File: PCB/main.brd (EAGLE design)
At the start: 98.1 x 68.5 mm, 81 parts, among them X1 BU-SMA-V

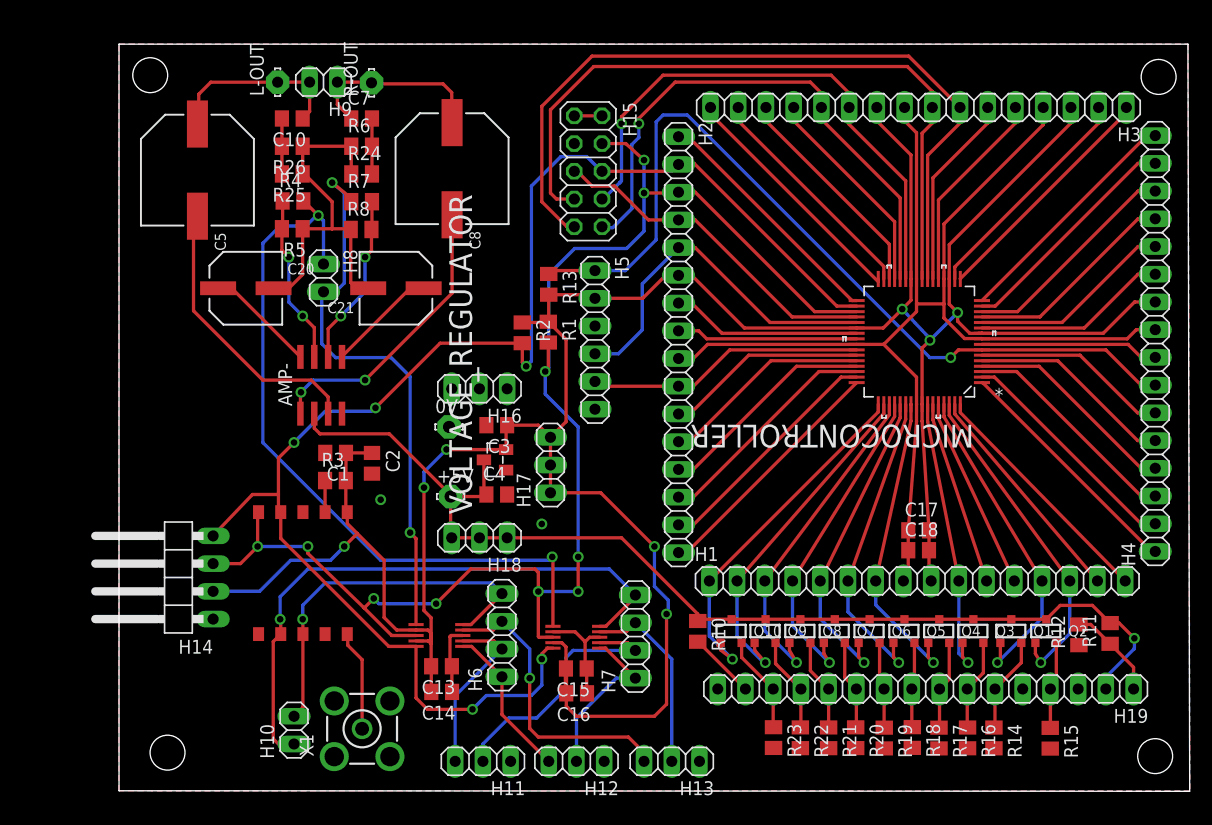
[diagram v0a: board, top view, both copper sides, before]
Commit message: "Final" PCB changes
Changes from group PCB review
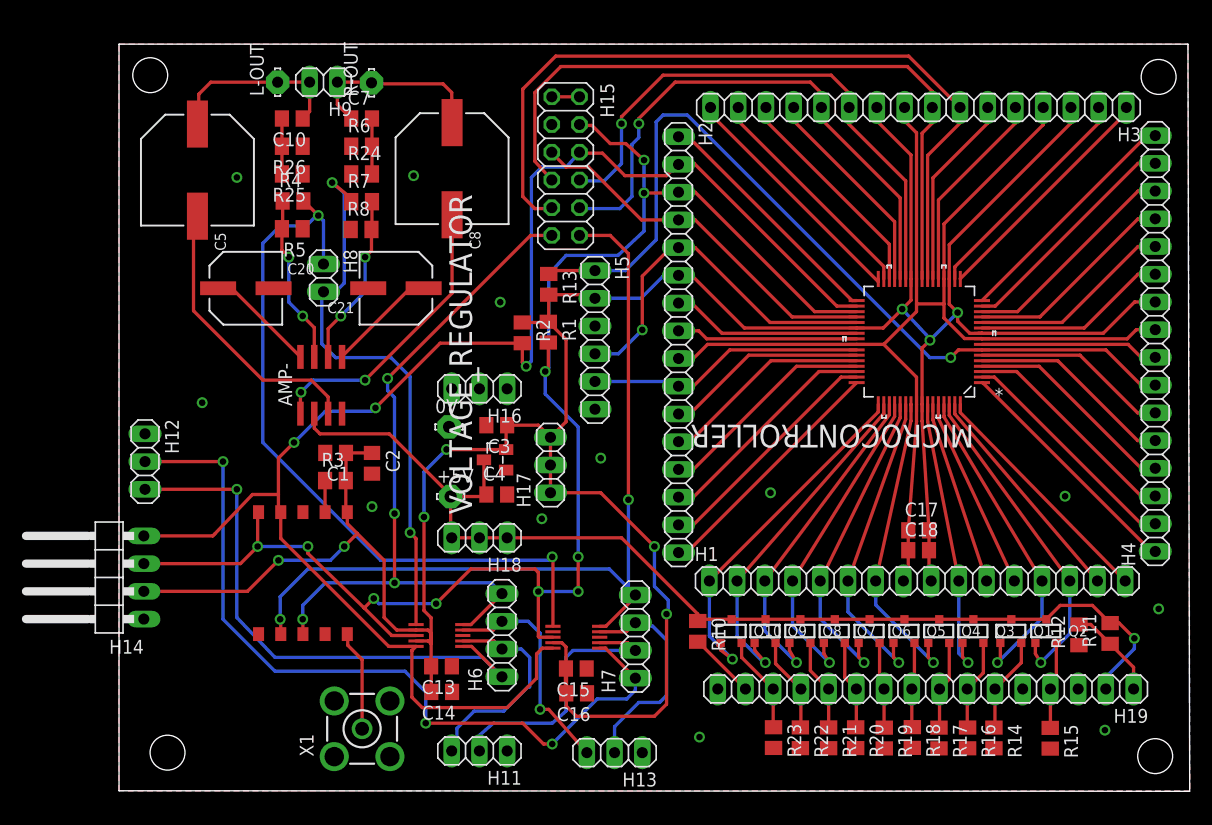
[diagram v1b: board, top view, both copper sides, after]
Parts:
- removed H10: (no value), pinhead:1X02
- H15: device pinhead:2X05 -> pinhead:2X06
- moved H12 48.1 mm to (4.29, 30.2), turned to 270 degrees
- moved H14 6.35 mm to (0.36, 19.5)
- moved H13 5.30 mm to (47.3, 3.49)
- moved H15 2.12 mm to (42.8, 57.2)
- moved H11 1.00 mm to (34.9, 3.65)
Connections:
- net FM-L: now also H15.11; no longer H10.2
- net FM-R: now also H15.12; no longer H10.1
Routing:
- net BT-R: track 15.3 -> 73.3 mm, vias 0 -> 3
- net GND: track 161.4 -> 114.1 mm
- net BT-L: track 14.3 -> 51.5 mm, vias 0 -> 1
- net FM-L: track 34.8 -> 66.4 mm, vias 1 -> 4
- net FM-R: track 54.6 -> 79.3 mm, vias 1 -> 2
- net SDA/MISO: track 133.5 -> 142.7 mm
- net SCL: track 136.1 -> 143.6 mm, vias 5 -> 3
- net +3V3: track 273.3 -> 279.7 mm, vias 8 -> 9
- net REC-L: track 27.0 -> 21.3 mm
- net AUX-L: track 16.0 -> 20.0 mm
- net REC-R: track 17.7 -> 20.5 mm
- net MOSI: track 31.4 -> 34.2 mm
- net XCS: track 71.9 -> 73.4 mm
- net AUX-R: track 24.3 -> 25.3 mm
- net XDCS: track 50.6 -> 51.2 mm
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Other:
- board text added: "3v3"
- board text added: "5v"
- board text added: "5v Input"
- board text added: "AMP-L"
- board text added: "AMP-R"
- board text added: "AUX-L"
- board text added: "AUX-R"
- board text added: "BT-L"
- board text added: "BT-R"
- board text added: "CNTRST"
- board text added: "D0"
- board text added: "D7"
- board text added: "DREQ"
- board text added: "E"
- board text added: "EEE2037 LDPS IV FM Receiver Project"
- board text added: "FM-L"
- board text added: "FM-R"
- board text added: "GND"
- board text added: "Ground"
- board text added: "LED+"
- board text added: "LED-"
- board text added: "MISO"
- board text added: "MOSI"
- board text added: "OUT-L"
- board text added: "OUT-R"
- board text added: "Output-L"
- board text added: "Output-R"
- board text added: "PICkit"
- board text added: "R/W"
- board text added: "REC-L"
- board text added: "REC-R"
- board text added: "RS"
- board text added: "SCL"
- board text added: "SDA"
- board text added: "Sebastian Goscik Phil Handley Stuart Rayner"
- board text added: "XCS"
- board text added: "XDCS"
- board text added: "XRST"
- board text added: "^"

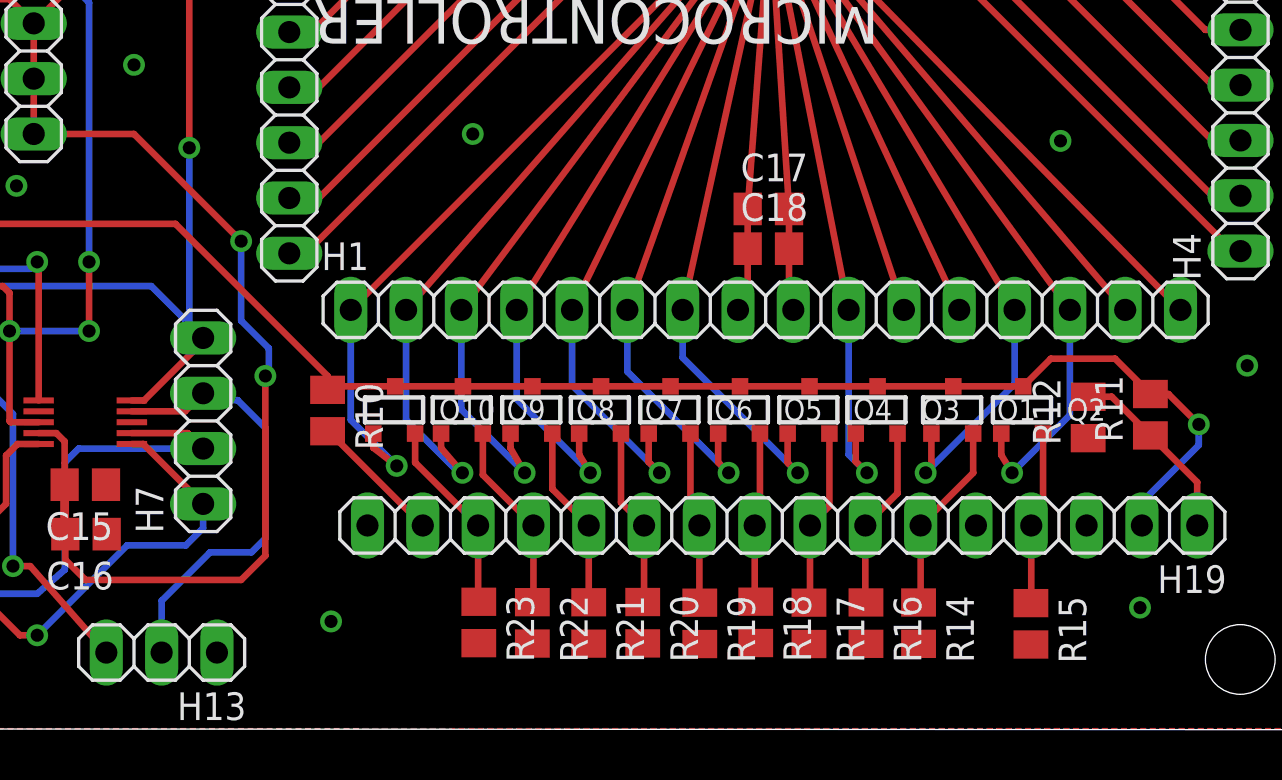
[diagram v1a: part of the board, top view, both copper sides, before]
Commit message: FINAL! PCB changes
- Keep out for ground plane inside PIC fanout
- Connected ground vias to ground net
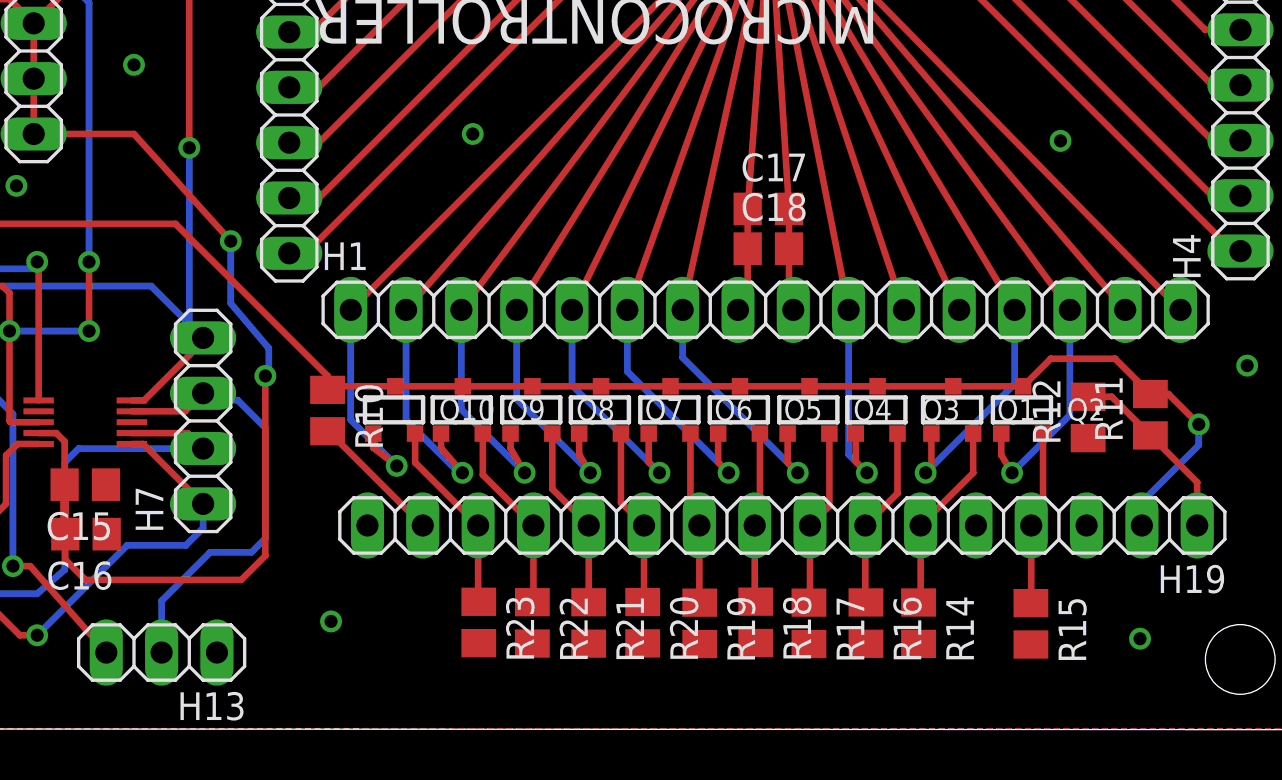
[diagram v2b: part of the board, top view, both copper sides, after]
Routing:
- net GND: vias 2 -> 12
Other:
- board text added: "CTR"
- board text removed: "CNTRST"
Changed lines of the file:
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@@
 <text x="87.9475" y="7.3025" size="1.27" layer="100" rot="MR270">RS</text>
 <text x="85.24875" y="7.14375" size="1.27" layer="100" rot="MR270">R/W</text>
-<text x="93.0275" y="7.3025" size="1.27" layer="100" rot="MR270">5v</text>
-<text x="94.77375" y="7.77875" size="1.27" layer="100" rot="MR270">CNTRST</text>
+<text x="92.86875" y="7.3025" size="1.27" layer="100" rot="MR270">5v</text>
+<text x="94.615" y="7.3025" size="1.27" layer="100" rot="MR270">CTR</text>
 <text x="40.48125" y="63.02375" size="1.27" layer="100" rot="MR0">5v</text>
 <text x="46.99" y="63.02375" size="1.27" layer="100" rot="MR0">5v</text>
@@
 <text x="6.985" y="34.6075" size="1.27" layer="101" rot="R90">EEE2037 LDPS IV
 FM Receiver Project</text>
+<polygon width="0.3048" layer="41">
+<vertex x="53.49875" y="23.8125"/>
+<vertex x="53.18125" y="23.8125"/>
+<vertex x="53.18125" y="53.0225"/>
+<vertex x="55.40375" y="53.0225"/>
+<vertex x="68.10375" y="40.3225"/>
+<vertex x="68.10375" y="37.30625"/>
+<vertex x="54.9275" y="24.13"/>
+<vertex x="53.49875" y="24.13"/>
+<vertex x="53.34" y="23.97125"/>
+</polygon>
+<polygon width="0.3048" layer="41">
+<vertex x="67.46875" y="62.07125"/>
+<vertex x="67.46875" y="59.53125"/>
+<vertex x="78.58125" y="48.41875"/>
+<vertex x="79.53375" y="48.41875"/>
+<vertex x="93.18625" y="62.07125"/>
+<vertex x="67.6275" y="62.07125"/>
+</polygon>
+<polygon width="0.3048" layer="41">
+<vertex x="96.52" y="60.325"/>
+<vertex x="96.52" y="24.4475"/>
+<vertex x="96.2025" y="24.13"/>
+<vertex x="95.25" y="24.13"/>
+<vertex x="81.915" y="37.465"/>
+<vertex x="81.915" y="44.92625"/>
+<vertex x="96.8375" y="59.84875"/>
+<vertex x="96.8375" y="60.0075"/>
+</polygon>
+<polygon width="0.3048" layer="41">
+<vertex x="66.19875" y="19.3675"/>
+<vertex x="71.12" y="19.3675"/>
+<vertex x="71.59625" y="19.84375"/>
+<vertex x="73.3425" y="29.05125"/>
+<vertex x="69.37375" y="27.94"/>
+<vertex x="66.19875" y="19.20875"/>
+</polygon>
+<polygon width="0.3048" layer="41">
+<vertex x="74.13625" y="21.2725"/>
+<vertex x="76.67625" y="21.2725"/>
+<vertex x="77.1525" y="28.8925"/>
+<vertex x="80.3275" y="27.78125"/>
+<vertex x="84.29625" y="19.52625"/>
+<vertex x="73.9775" y="19.685"/>
+</polygon>
+<polygon width="0.3048" layer="41">
+<vertex x="72.54875" y="24.765"/>
+<vertex x="77.1525" y="24.92375"/>
+<vertex x="77.1525" y="28.8925"/>
+<vertex x="73.18375" y="29.05125"/>
+</polygon>
+<polygon width="0.3048" layer="41">
+<vertex x="67.46875" y="66.3575"/>
+<vertex x="67.945" y="63.5"/>
+<vertex x="76.67625" y="63.1825"/>
+<vertex x="76.04125" y="65.56375"/>
+</polygon>
 </plain>
 <attributes>
@@
 <wire x1="42.8625" y1="41.345" x2="41.23625" y2="42.97125" width="0.3048" layer="1"/>
 <wire x1="41.43375" y1="27.305" x2="46.0375" y2="27.305" width="0.3048" layer="1"/>
-<wire x1="46.0375" y1="27.305" x2="50.95875" y2="22.38375" width="0.3048" layer="1"/>
-<via x="50.95875" y="22.38375" extent="1-16" drill="0.6" shape="square"/>
-<wire x1="50.95875" y1="22.38375" x2="50.95875" y2="18.7325" width="0.3048" layer="16"/>
-<wire x1="50.95875" y1="18.7325" x2="52.22875" y2="17.4625" width="0.3048" layer="16"/>
+<wire x1="46.0375" y1="27.305" x2="50.4825" y2="22.38375" width="0.3048" layer="1"/>
+<via x="50.4825" y="22.38375" extent="1-16" drill="0.6" shape="square"/>
+<wire x1="50.4825" y1="22.38375" x2="50.4825" y2="19.52625" width="0.3048" layer="16"/>
+<wire x1="50.4825" y1="19.52625" x2="52.22875" y2="17.4625" width="0.3048" layer="16"/>
 <wire x1="52.22875" y1="17.4625" x2="52.22875" y2="16.35125" width="0.3048" layer="16"/>
 <wire x1="52.22875" y1="16.35125" x2="52.07" y2="16.1925" width="0.3048" layer="16"/>
@@
 <wire x1="74.21675" y1="23.8635" x2="74.9735" y2="33.82775" width="0.3048" layer="1"/>
 <wire x1="74.9735" y1="33.82775" x2="74.9735" y2="35.4146" width="0.3048" layer="1"/>
+<via x="9.525" y="35.56" extent="1-16" drill="0.6" shape="square"/>
+<via x="12.7" y="56.1975" extent="1-16" drill="0.6" shape="square"/>
+<via x="28.8925" y="56.35625" extent="1-16" drill="0.6" shape="square"/>
+<via x="46.0375" y="30.48" extent="1-16" drill="0.6" shape="square"/>
+<via x="97.155" y="16.66875" extent="1-16" drill="0.6" shape="square"/>
+<via x="55.08625" y="4.92125" extent="1-16" drill="0.6" shape="square"/>
+<via x="88.5825" y="26.9875" extent="1-16" drill="0.6" shape="square"/>
+<via x="61.595" y="27.305" extent="1-16" drill="0.6" shape="square"/>
+<via x="36.83" y="44.7675" extent="1-16" drill="0.6" shape="square"/>
+<via x="92.23375" y="4.1275" extent="1-16" drill="0.6" shape="square"/>
 <wire x1="44.60875" y1="11.345" x2="45.94" y2="14.06875" width="0" layer="19" extent="1-1"/>
 <wire x1="41.66" y1="14.56875" x2="45.94" y2="14.06875" width="0" layer="19" extent="1-1"/>
@@
 <wire x1="53.9163" y1="21.825" x2="69.4871" y2="37.3958" width="0.3048" layer="1"/>
 </signal>
-<signal name="N$2">
-<via x="12.7" y="56.1975" extent="1-16" drill="0.6" shape="square"/>
-</signal>
-<signal name="N$6">
-<via x="28.8925" y="56.35625" extent="1-16" drill="0.6" shape="square"/>
-</signal>
-<signal name="N$9">
-<via x="9.525" y="35.56" extent="1-16" drill="0.6" shape="square"/>
-</signal>
-<signal name="N$11">
-<via x="55.08625" y="4.92125" extent="1-16" drill="0.6" shape="square"/>
-</signal>
-<signal name="N$12">
-<via x="92.23375" y="5.55625" extent="1-16" drill="0.6" shape="square"/>
-</signal>
-<signal name="N$15">
-<via x="97.155" y="16.66875" extent="1-16" drill="0.6" shape="square"/>
-</signal>
-<signal name="N$16">
-<via x="88.5825" y="26.9875" extent="1-16" drill="0.6" shape="square"/>
-</signal>
-<signal name="N$19">
-<via x="61.595" y="27.305" extent="1-16" drill="0.6" shape="square"/>
-</signal>
-<signal name="N$21">
-<via x="46.0375" y="30.48" extent="1-16" drill="0.6" shape="square"/>
-</signal>
-<signal name="N$22">
-<via x="36.83" y="44.7675" extent="1-16" drill="0.6" shape="square"/>
-</signal>
 </signals>
